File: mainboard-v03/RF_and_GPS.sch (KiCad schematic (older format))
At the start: 15 parts, among them J11 Conn_01x02, J5 Conn_Coaxial, J6 Conn_Coaxial, J7 Conn_Coaxial, U10 XTB-40, U11 XTB-40, U12 XTB-40, U13 EP2W+, U14 S1216V8, U23 RFM98PW, U9 XTB-40

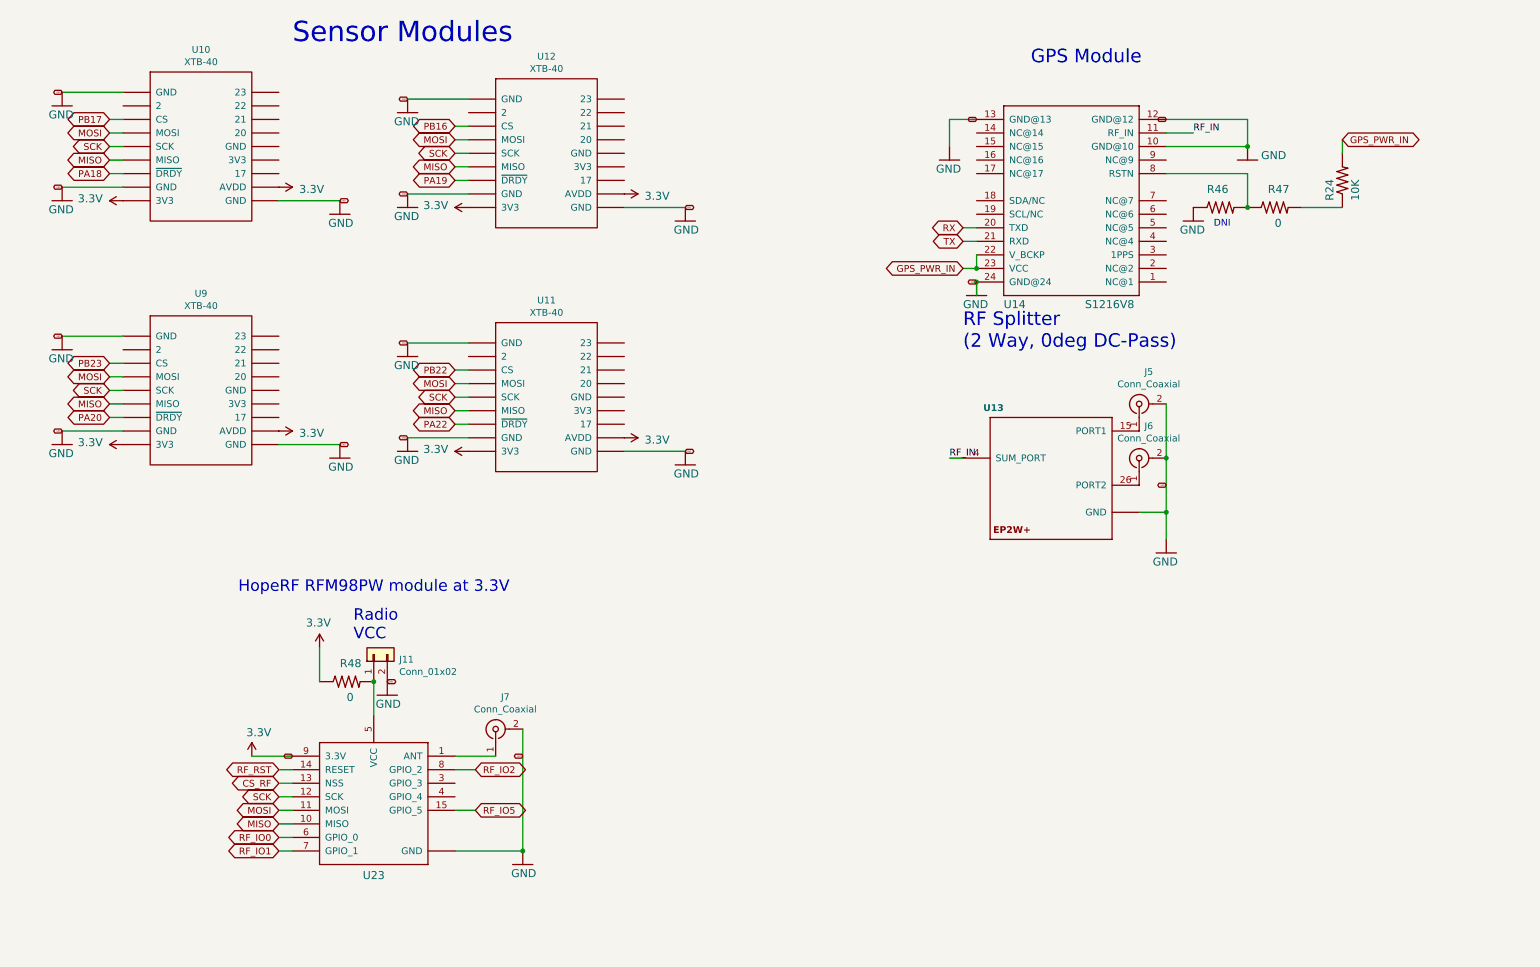
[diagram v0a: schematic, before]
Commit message: cleaning up schematic scheets
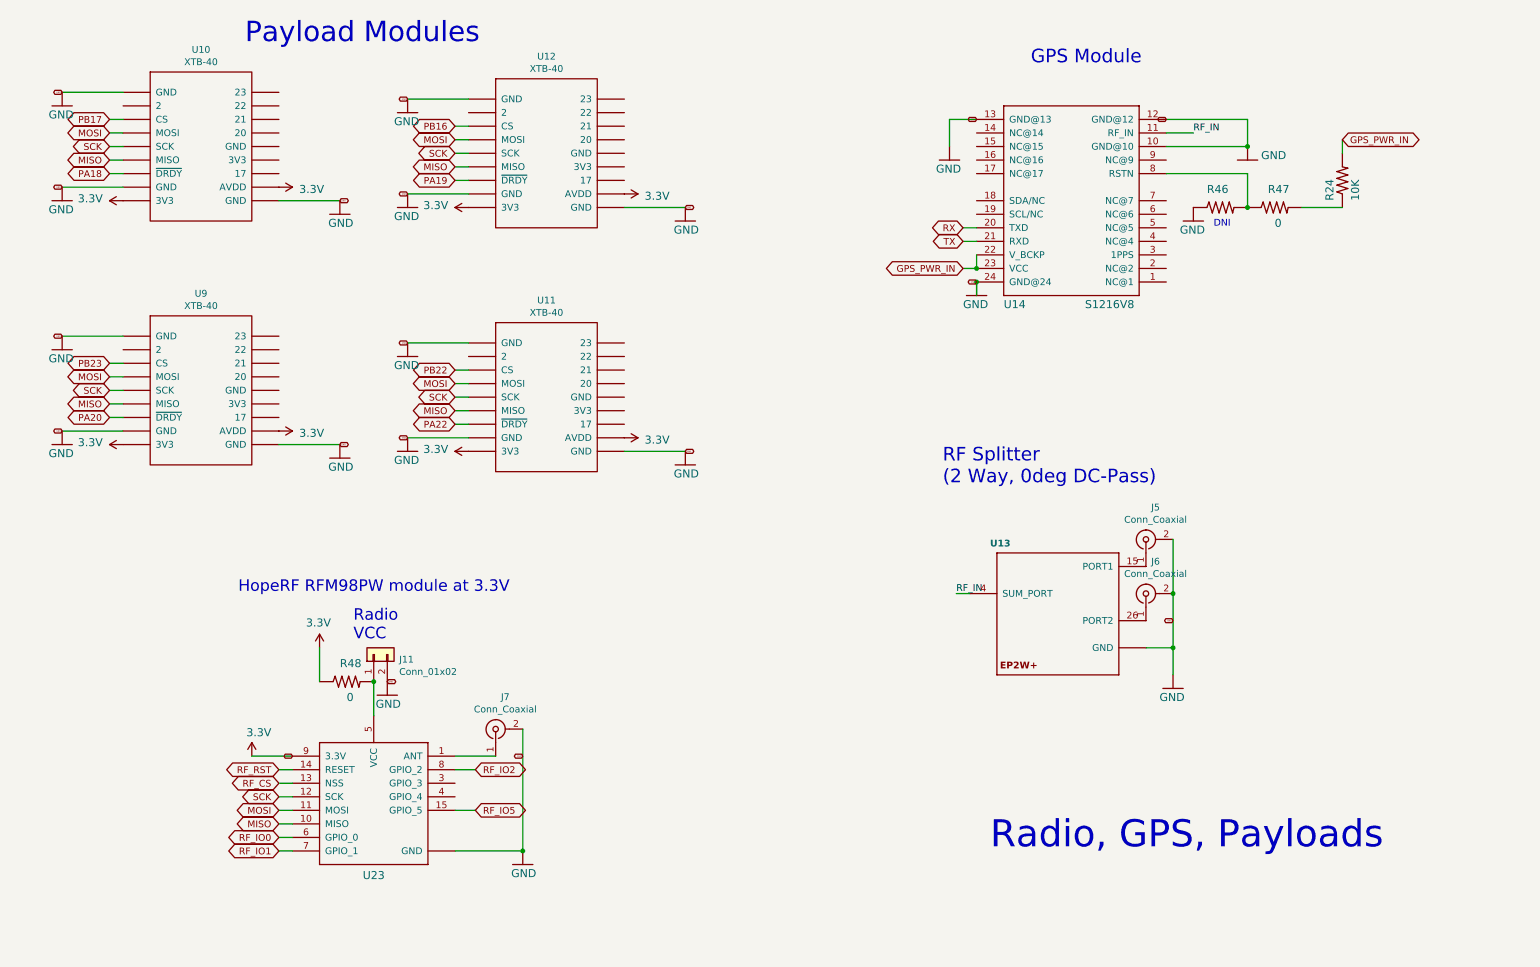
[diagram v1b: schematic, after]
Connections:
- net CS_RF renamed RF_CS
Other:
- note added: "Payload Modules"
- note added: "Radio, GPS, Payloads"
- note removed: "Sensor Modules"
- moved on the sheet: J5, J6, U13
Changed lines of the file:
@@
 $Descr A4 11693 8268
 encoding utf-8
-Sheet 5 6
+Sheet 3 6
 Title "PyCubed Mainboard"
 Date ""
-Rev "v02"
+Rev "v03"
 Comp "Stanford University"
 Comment1 "rexlab.stanford.edu"
@@
 GND
 Wire Wire Line
-	9200 4500 9200 4700
-Wire Wire Line
-	9000 4500 9200 4500
-Connection ~ 9200 4500
-Text GLabel 9200 4300 0    10   BiDi ~ 0
+	9250 5500 9250 5700
+Wire Wire Line
+	9050 5500 9250 5500
+Connection ~ 9250 5500
+Text GLabel 9250 5300 0    10   BiDi ~ 0
 GND
 Wire Wire Line
@@
 RF_IN
 Wire Wire Line
-	7700 4100 7600 4100
-Text Label 7600 4100 0    50   ~ 0
+	7750 5100 7650 5100
+Text Label 7650 5100 0    50   ~ 0
 RF_IN
 Wire Wire Line
@@
 L mainboard:EP2W+ U?
 U 1 0 6D2AEAA6
-P 8400 4100
+P 8450 5100
 AR Path="/6D2AEAA6" Ref="U?"  Part="1"
 AR Path="/5CEC6281/6D2AEAA6" Ref="U13"  Part="1"
-F 0 "U13" H 8000 4500 50  0000 R TNB
-F 1 "EP2W+" H 8400 4100 50  0001 C CNN
-F 2 "kmb-test:QFN32-5X5MM" H 8400 4100 50  0001 C CNN
-F 3 "" H 8400 4100 50  0001 C CNN
-	1    8400 4100
+F 0 "U13" H 8050 5500 50  0000 R TNB
+F 1 "EP2W+" H 8450 5100 50  0001 C CNN
+F 2 "kmb-test:QFN32-5X5MM" H 8450 5100 50  0001 C CNN
+F 3 "" H 8450 5100 50  0001 C CNN
+	1    8450 5100
 	1    0    0    -1
 $EndComp
@@
 L mainboard:GND #GND?
 U 1 0 5123C17D
-P 9200 4800
+P 9250 5800
 AR Path="/5123C17D" Ref="#GND?"  Part="1"
 AR Path="/5CEC6281/5123C17D" Ref="#GND044"  Part="1"
-F 0 "#GND044" H 9200 4800 50  0001 C CNN
-F 1 "GND" H 9100 4700 59  0000 L BNN
-F 2 "" H 9200 4800 50  0001 C CNN
-F 3 "" H 9200 4800 50  0001 C CNN
-	1    9200 4800
+F 0 "#GND044" H 9250 5800 50  0001 C CNN
+F 1 "GND" H 9150 5700 59  0000 L BNN
+F 2 "" H 9250 5800 50  0001 C CNN
+F 3 "" H 9250 5800 50  0001 C CNN
+	1    9250 5800
 	1    0    0    -1
 $EndComp
@@
 Text Notes 2350 5100 0    85   ~ 0
 HopeRF RFM98PW module at 3.3V
-Text Notes 7700 3300 0    100  ~ 0
-RF Splitter \n(2 Way, 0deg DC-Pass)
-Text Notes 2750 1050 0    150  ~ 0
-Sensor Modules
+Text Notes 7550 4300 0    100  ~ 0
+       RF Splitter \n(2 Way, 0deg DC-Pass)
+Text Notes 2400 1050 0    150  ~ 0
+Payload Modules
 $Comp
 L Connector:Conn_Coaxial J5
 U 1 1 5D3A148B
-P 9000 3700
-F 0 "J5" V 9237 3629 50  0000 C CNN
-F 1 "Conn_Coaxial" V 9146 3629 50  0000 C CNN
-F 2 "Connector_Coaxial:SMA_Amphenol_901-144_Vertical" H 9000 3700 50  0001 C CNN
-F 3 " ~" H 9000 3700 50  0001 C CNN
-	1    9000 3700
+P 9050 4700
+F 0 "J5" V 9287 4629 50  0000 C CNN
+F 1 "Conn_Coaxial" V 9196 4629 50  0000 C CNN
+F 2 "Connector_Coaxial:SMA_Amphenol_901-144_Vertical" H 9050 4700 50  0001 C CNN
+F 3 " ~" H 9050 4700 50  0001 C CNN
+	1    9050 4700
 	0    -1   -1   0
 $EndComp
 Wire Wire Line
-	9200 3700 9200 4100
+	9250 4700 9250 5100
 $Comp
 L Connector:Conn_Coaxial J6
 U 1 1 5D3A5B0D
-P 9000 4100
-F 0 "J6" V 9237 4029 50  0000 C CNN
-F 1 "Conn_Coaxial" V 9146 4029 50  0000 C CNN
-F 2 "Connector_Coaxial:SMA_Amphenol_901-144_Vertical" H 9000 4100 50  0001 C CNN
-F 3 " ~" H 9000 4100 50  0001 C CNN
-	1    9000 4100
+P 9050 5100
+F 0 "J6" V 9287 5029 50  0000 C CNN
+F 1 "Conn_Coaxial" V 9196 5029 50  0000 C CNN
+F 2 "Connector_Coaxial:SMA_Amphenol_901-144_Vertical" H 9050 5100 50  0001 C CNN
+F 3 " ~" H 9050 5100 50  0001 C CNN
+	1    9050 5100
 	0    -1   -1   0
 $EndComp
-Connection ~ 9200 4100
-Wire Wire Line
-	9200 4100 9200 4500
+Connection ~ 9250 5100
+Wire Wire Line
+	9250 5100 9250 5500
 $Comp
 L Connector:Conn_Coaxial J7
@@
 	2750 6500 2650 6500
 Text GLabel 2650 6500 0    50   BiDi ~ 0
-CS_RF
+RF_CS
 Wire Wire Line
 	3950 7000 4450 7000
@@
 Text GLabel 3450 5750 2    10   BiDi ~ 0
 GND
+Text Notes 7900 7000 0    200  ~ 0
+Radio, GPS, Payloads
 $EndSCHEMATC

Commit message: mainboardv3 clean up
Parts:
- added J12: Conn_Coaxial, Connector_Coaxial:SMA_Amphenol_901-144_Vertical, symbol Connector:Conn_Coaxial
- added U15, U20: RFM9xBreakout, RF_Module:HOPERF_RFM9XW_SMD, symbol symbols:RFM9xBreakout
- added U24: RFM98PW, custom-footprints:RFM98PW, symbol symbols:RFM98PW
- U13: footprint kmb-test:QFN32-5X5MM -> mainboard:QFN32-5X5MM
- U14: footprint kmb-test:S1216_24PIN_PACKAGE -> mainboard:S1216_24PIN_PACKAGE
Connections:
- net GND: now also J12.2 (Ext), U15.1 (GND), U15.10 (GND), U15.8 (GND), U20.1 (GND), U20.10 (GND), U20.8 (GND), U24.16 (GND), U24.2 (GND)
- net MISO: now also U15.2 (MISO), U20.2 (MISO), U24.10 (MISO)
- net MOSI: now also U15.3 (MOSI), U20.3 (MOSI), U24.11 (MOSI)
- net SCK: now also U15.4 (SCK), U20.4 (SCK), U24.12 (SCK)
- net RF1_ANT: now reaches J7.1 (In), U23.1 (ANT)
- net RF1_ANT: now also U20.9 (ANT)
- net RF1_IO4: now reaches U23.4 (GPIO_4)
- net RF1_IO4: now also U20.12 (BUSY)
- net at J11.1 (Pin_1), R48.2, U23.5 (VCC): now also U20.13 (3V3)
- net RF_CS renamed RF1_CS
- net RF1_CS: now also U20.5 (CS)
- net RF_IO0 renamed RF1_IO0
- net RF1_IO0: now also U15.14 (DIO0), U20.14 (DIO0), U24.6 (GPIO_0)
- net RF_IO1 renamed RF1_IO1
- net RF1_IO1: now also U20.15 (DIO1)
- net RF_IO2 renamed RF1_IO2
- net RF1_IO2: now also U20.16 (DIO2)
- net RF_IO5: no longer names the net of U23.15 (GPIO_5)
- net RF_RST renamed RF1_RST
- net RF1_RST: now also U20.6 (~RESET)
- new net: U24.5 (VCC), U24.9 (3.3V)
- new net RF2_ANT: J12.1 (In), U15.9 (ANT), U24.1 (ANT)
- new net RF2_BUSY: U15.12 (BUSY), U24.4 (GPIO_4)
- new net RF2_CS: U15.5 (CS), U24.13 (NSS)
- new net RF2_IO1: U15.15 (DIO1), U24.7 (GPIO_1)
- new net RF2_IO2: U15.16 (DIO2), U24.8 (GPIO_2)
- new net RF2_RST: U15.6 (~RESET), U24.14 (RESET)
- no-connect marks 0 -> 2
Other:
- moved on the sheet: J11, J7, U23
